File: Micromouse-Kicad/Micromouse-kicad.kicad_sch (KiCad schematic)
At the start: 67 parts, among them J1 UARTBTH, J2 Batería, J3 VL6180x, J4 MotorEncodL, J5 MotorEncodR, Q1 BS170, Q2 BS170, Q3 BS170, Q4 BS170, SW1 PowerSwitch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

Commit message: Esquemático simplificado
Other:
- note added: "Led externo y botón extra"
- note added: "Medidor - Voltaje en batería"
- note removed: "Botón Extra"
- note removed: "LEDS"
- note removed: "Voltaje Batería"
- moved on the sheet: C1, C2, C3, C4, C5, C6, C7, C8, CBOT1, CD1, CD2, CM1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

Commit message: Micromouse con Blackpill routeado!
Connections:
- net ML1: now also U1.7 (PA10); no longer U1.5 (PA8)
- net MR1: now also U1.37 (PB10); no longer U1.7 (PA10)
- net MR2: now also U1.5 (PA8); no longer U1.37 (PB10)
- net OutML1: now also J5.6 (Pin_6); no longer J4.6 (Pin_6)
- net OutML2: now also J5.5 (Pin_5); no longer J4.5 (Pin_5)
- net OutMR1: now also J4.5 (Pin_5); no longer J5.6 (Pin_6)
- net OutMR2: now also J4.6 (Pin_6); no longer J5.5 (Pin_5)
- net TIM3_CH1: now also J4.2 (Pin_2); no longer J4.3 (Pin_3)
- net TIM3_CH2: now also J4.3 (Pin_3); no longer J4.2 (Pin_2)
- net TIM4_CH1: now also J5.2 (Pin_2); no longer J5.3 (Pin_3)
- net TIM4_CH2: now also J5.3 (Pin_3); no longer J5.2 (Pin_2)
- net Vdrive: no longer U1.18 (5V)
- no-connect marks 24 -> 25
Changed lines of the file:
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@@
   (no_connect (at 30.48 30.48))
   (no_connect (at 30.48 45.72))
+  (no_connect (at 30.48 68.58))
   (no_connect (at 30.48 43.18))
   (no_connect (at 157.48 40.64))
@@
     )
   )
-  (global_label "TIM3_CH1" (shape input) (at 152.4 139.7 180) (fields_autoplaced)
+  (global_label "TIM3_CH1" (shape input) (at 152.4 137.16 180) (fields_autoplaced)
     (effects (font (size 1.27 1.27)) (justify right))
-    (property "Intersheet References" "${INTERSHEET_REFS}" (id 0) (at 140.9759 139.6206 0)
+    (property "Intersheet References" "${INTERSHEET_REFS}" (id 0) (at 140.9759 137.0806 0)
       (effects (font (size 1.27 1.27)) (justify right) hide)
     )
@@
     )
   )
-  (global_label "OutML1" (shape input) (at 152.4 147.32 180) (fields_autoplaced)
+  (global_label "OutML1" (shape input) (at 152.4 167.64 180) (fields_autoplaced)
     (effects (font (size 1.27 1.27)) (justify right))
-    (property "Intersheet References" "${INTERSHEET_REFS}" (id 0) (at 143.0926 147.3994 0)
+    (property "Intersheet References" "${INTERSHEET_REFS}" (id 0) (at 143.0926 167.7194 0)
       (effects (font (size 1.27 1.27)) (justify right) hide)
     )
@@
     )
   )
-  (global_label "OutMR2" (shape input) (at 152.4 165.1 180) (fields_autoplaced)
+  (global_label "OutMR2" (shape input) (at 152.4 147.32 180) (fields_autoplaced)
     (effects (font (size 1.27 1.27)) (justify right))
-    (property "Intersheet References" "${INTERSHEET_REFS}" (id 0) (at 142.8507 165.0206 0)
+    (property "Intersheet References" "${INTERSHEET_REFS}" (id 0) (at 142.8507 147.2406 0)
       (effects (font (size 1.27 1.27)) (justify right) hide)
     )
@@
     )
   )
-  (global_label "OutML2" (shape input) (at 152.4 144.78 180) (fields_autoplaced)
+  (global_label "OutML2" (shape input) (at 152.4 165.1 180) (fields_autoplaced)
     (effects (font (size 1.27 1.27)) (justify right))
-    (property "Intersheet References" "${INTERSHEET_REFS}" (id 0) (at 143.0926 144.8594 0)
+    (property "Intersheet References" "${INTERSHEET_REFS}" (id 0) (at 143.0926 165.1794 0)
       (effects (font (size 1.27 1.27)) (justify right) hide)
     )
@@
     )
   )
-  (global_label "ML1" (shape input) (at 30.48 35.56 180) (fields_autoplaced)
+  (global_label "ML1" (shape input) (at 30.48 40.64 180) (fields_autoplaced)
     (effects (font (size 1.27 1.27)) (justify right))
-    (property "Intersheet References" "${INTERSHEET_REFS}" (id 0) (at 24.3779 35.6394 0)
+    (property "Intersheet References" "${INTERSHEET_REFS}" (id 0) (at 24.3779 40.7194 0)
       (effects (font (size 1.27 1.27)) (justify right) hide)
     )
@@
     )
   )
-  (global_label "TIM4_CH2" (shape input) (at 152.4 157.48 180) (fields_autoplaced)
+  (global_label "TIM4_CH2" (shape input) (at 152.4 160.02 180) (fields_autoplaced)
     (effects (font (size 1.27 1.27)) (justify right))
-    (property "Intersheet References" "${INTERSHEET_REFS}" (id 0) (at 140.9759 157.4006 0)
+    (property "Intersheet References" "${INTERSHEET_REFS}" (id 0) (at 140.9759 159.9406 0)
       (effects (font (size 1.27 1.27)) (justify right) hide)
     )
@@
     )
   )
-  (global_label "TIM4_CH1" (shape input) (at 152.4 160.02 180) (fields_autoplaced)
+  (global_label "TIM4_CH1" (shape input) (at 152.4 157.48 180) (fields_autoplaced)
     (effects (font (size 1.27 1.27)) (justify right))
-    (property "Intersheet References" "${INTERSHEET_REFS}" (id 0) (at 140.9759 159.9406 0)
+    (property "Intersheet References" "${INTERSHEET_REFS}" (id 0) (at 140.9759 157.4006 0)
       (effects (font (size 1.27 1.27)) (justify right) hide)
     )
@@
     )
   )
-  (global_label "MR1" (shape input) (at 30.48 40.64 180) (fields_autoplaced)
-    (effects (font (size 1.27 1.27)) (justify right))
-    (property "Intersheet References" "${INTERSHEET_REFS}" (id 0) (at 24.1359 40.7194 0)
-      (effects (font (size 1.27 1.27)) (justify right) hide)
+  (global_label "MR1" (shape input) (at 71.12 33.02 0) (fields_autoplaced)
+    (effects (font (size 1.27 1.27)) (justify left))
+    (property "Intersheet References" "${INTERSHEET_REFS}" (id 0) (at 77.4641 32.9406 0)
+      (effects (font (size 1.27 1.27)) (justify left) hide)
     )
   )
@@
     )
   )
-  (global_label "TIM3_CH2" (shape input) (at 152.4 137.16 180) (fields_autoplaced)
+  (global_label "TIM3_CH2" (shape input) (at 152.4 139.7 180) (fields_autoplaced)
     (effects (font (size 1.27 1.27)) (justify right))
-    (property "Intersheet References" "${INTERSHEET_REFS}" (id 0) (at 140.9759 137.0806 0)
+    (property "Intersheet References" "${INTERSHEET_REFS}" (id 0) (at 140.9759 139.6206 0)
       (effects (font (size 1.27 1.27)) (justify right) hide)
     )
   )
-  (global_label "OutMR1" (shape input) (at 152.4 167.64 180) (fields_autoplaced)
+  (global_label "OutMR1" (shape input) (at 152.4 144.78 180) (fields_autoplaced)
     (effects (font (size 1.27 1.27)) (justify right))
-    (property "Intersheet References" "${INTERSHEET_REFS}" (id 0) (at 142.8507 167.5606 0)
+    (property "Intersheet References" "${INTERSHEET_REFS}" (id 0) (at 142.8507 144.7006 0)
       (effects (font (size 1.27 1.27)) (justify right) hide)
     )
@@
     )
   )
-  (global_label "MR2" (shape input) (at 71.12 33.02 0) (fields_autoplaced)
-    (effects (font (size 1.27 1.27)) (justify left))
-    (property "Intersheet References" "${INTERSHEET_REFS}" (id 0) (at 77.4641 32.9406 0)
-      (effects (font (size 1.27 1.27)) (justify left) hide)
+  (global_label "MR2" (shape input) (at 30.48 35.56 180) (fields_autoplaced)
+    (effects (font (size 1.27 1.27)) (justify right))
+    (property "Intersheet References" "${INTERSHEET_REFS}" (id 0) (at 24.1359 35.6394 0)
+      (effects (font (size 1.27 1.27)) (justify right) hide)
     )
   )
@@
     (pin "1")
   )
-  (symbol (lib_id "power:Vdrive") (at 30.48 68.58 90) (unit 1)
-    (in_bom yes) (on_board yes)
-    (property "Reference" "#PWR02" (id 0) (at 34.29 73.66 0)
-      (effects (font (size 1.27 1.27)) hide)
-    )
-    (property "Value" "Vdrive" (id 1) (at 21.59 68.58 90)
-      (effects (font (size 1.27 1.27)) (justify right))
-    )
-    (property "Footprint" "" (id 2) (at 30.48 68.58 0)
-      (effects (font (size 1.27 1.27)) hide)
-    )
-    (property "Datasheet" "" (id 3) (at 30.48 68.58 0)
-      (effects (font (size 1.27 1.27)) hide)
-    )
-    (pin "1")
-  )
   (symbol (lib_id "Device:R_Small") (at 212.09 125.73 180) (unit 1)
     (in_bom yes) (on_board yes) (fields_autoplaced)
@@
       (reference "#PWR01") (unit 1) (value "GND") (footprint "")
     )
-    (path "/05692abd-bb2d-49f8-9485-8f3ba7662f2d"
-      (reference "#PWR02") (unit 1) (value "Vdrive") (footprint "")
-    )
     (path "/b987dcaa-12bb-4caf-b0a2-4817a69f5312"

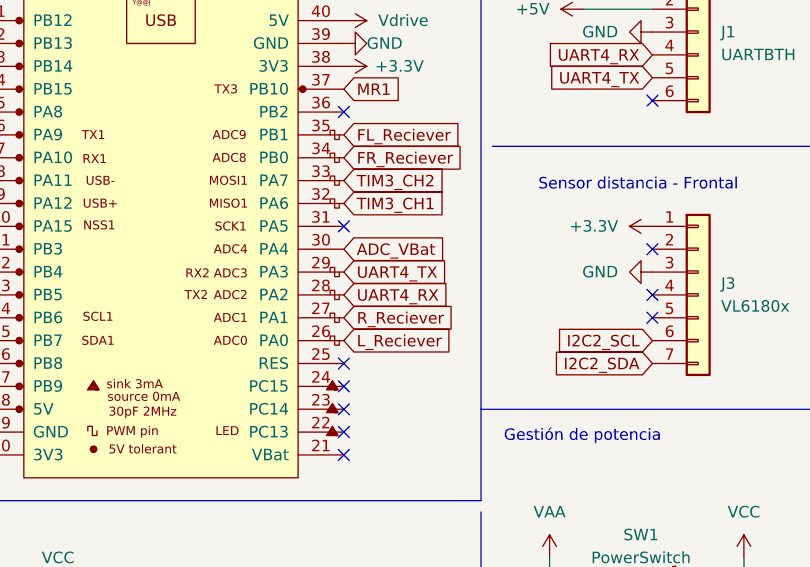
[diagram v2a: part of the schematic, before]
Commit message: Arreglo bluetooth
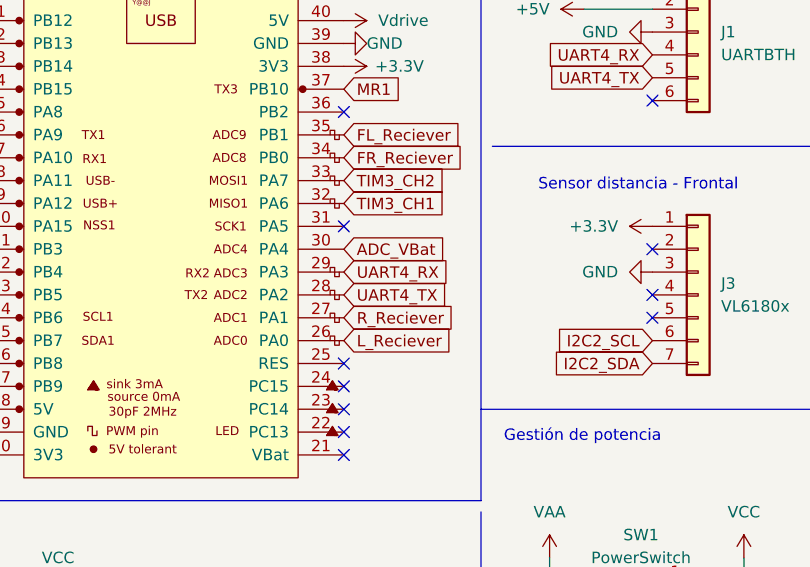
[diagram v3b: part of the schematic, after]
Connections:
- net UART4_RX: now also U1.29 (PA3); no longer U1.28 (PA2)
- net UART4_TX: now also U1.28 (PA2); no longer U1.29 (PA3)
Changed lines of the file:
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@@
     )
   )
-  (global_label "UART4_RX" (shape input) (at 71.12 55.88 0) (fields_autoplaced)
+  (global_label "UART4_RX" (shape input) (at 71.12 53.34 0) (fields_autoplaced)
     (effects (font (size 1.27 1.27)) (justify left))
-    (property "Intersheet References" "${INTERSHEET_REFS}" (id 0) (at 82.8464 55.8006 0)
+    (property "Intersheet References" "${INTERSHEET_REFS}" (id 0) (at 82.8464 53.2606 0)
       (effects (font (size 1.27 1.27)) (justify left) hide)
     )
@@
     )
   )
+  (global_label "UART4_TX" (shape input) (at 71.12 55.88 0) (fields_autoplaced)
+    (effects (font (size 1.27 1.27)) (justify left))
+    (property "Intersheet References" "${INTERSHEET_REFS}" (id 0) (at 82.5441 55.8006 0)
+      (effects (font (size 1.27 1.27)) (justify left) hide)
+    )
+  )
   (global_label "FL_Reciever" (shape input) (at 71.12 38.1 0) (fields_autoplaced)
     (effects (font (size 1.27 1.27)) (justify left))
@@
     )
   )
-  (global_label "UART4_TX" (shape input) (at 71.12 53.34 0) (fields_autoplaced)
-    (effects (font (size 1.27 1.27)) (justify left))
-    (property "Intersheet References" "${INTERSHEET_REFS}" (id 0) (at 82.5441 53.2606 0)
-      (effects (font (size 1.27 1.27)) (justify left) hide)
-    )
-  )
